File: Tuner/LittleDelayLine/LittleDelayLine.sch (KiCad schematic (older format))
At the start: 114 parts, among them J1 Conn_Coaxial, J10 Conn_Coaxial, J11 Conn_02x05_Odd_Even, J12 Conn_01x01, J13 Conn_01x01, J14 Conn_01x01, J15 Conn_01x01, J16 Conn_01x01, J17 Conn_Coaxial, J18 Conn_01x01, J19 Conn_01x01, J2 Conn_Coaxial, J20 Conn_01x01, J21 Conn_01x01, J22 Conn_Coaxial, J23 Conn_Coaxial, J24 Conn_Coaxial, J25 Conn_01x01, J26 Conn_01x01, J27 Conn_01x01, J3 Conn_Coaxial, J4 Conn_Coaxial, J5 Conn_Coaxial, J6 Conn_Coaxial, J7 Conn_Coaxial, J8 Conn_01x02, J9 Conn_01x02, P10 Conn_01x01, P11 Conn_01x01, P12 Conn_01x01, P2 Conn_01x01, P3 Conn_01x01, P4 Conn_01x01, P5 Conn_01x01, P6 Conn_01x01, P7 Conn_01x01, P8 Conn_01x01, P9 Conn_01x01, U1 MCP23008, U2 ULN2803A

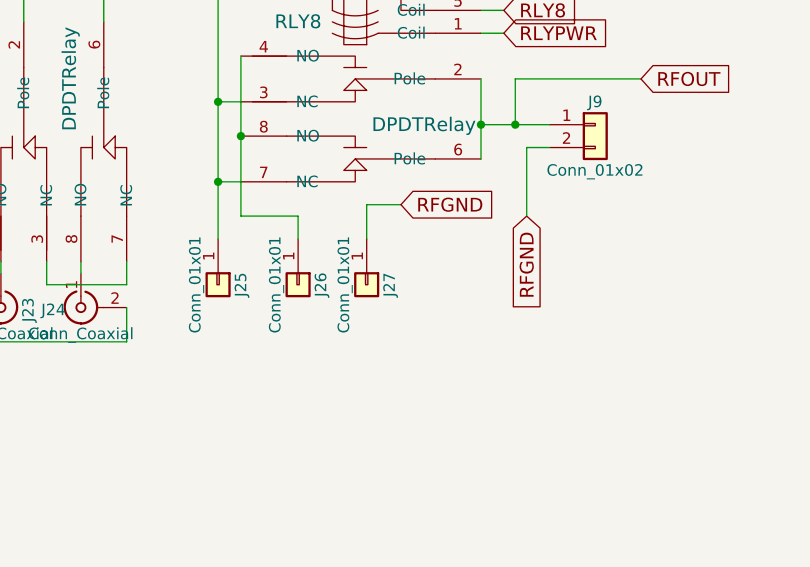
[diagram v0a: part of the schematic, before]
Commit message: Added more instrumentation to TandemMatch, fixed grounding issue
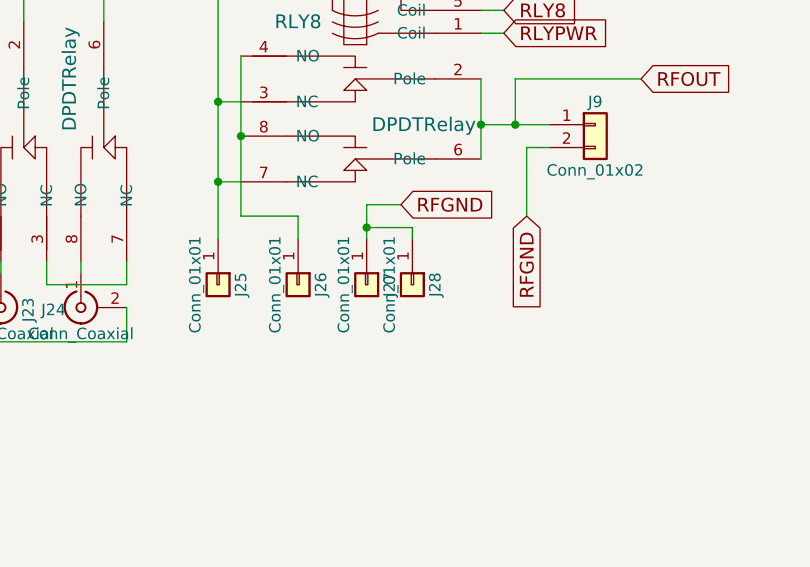
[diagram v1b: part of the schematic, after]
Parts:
- added J28: Conn_01x01, Connectors:1pin, symbol Conn_01x01
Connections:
- net RFGND: now also J28.1 (Pin_1)
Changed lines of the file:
@@
 	3150 4200 3300 4200
 Connection ~ 3300 4250
+$Comp
+L Conn_01x01 J28
+U 1 1 5C745726
+P 7950 2200
+F 0 "J28" H 7950 2300 50  0000 C CNN
+F 1 "Conn_01x01" H 7950 2100 50  0000 C CNN
+F 2 "Connectors:1pin" H 7950 2200 50  0001 C CNN
+F 3 "" H 7950 2200 50  0001 C CNN
+	1    7950 2200
+	0    1    1    0
+$EndComp
+Wire Wire Line
+	7950 2000 7950 1950
+Wire Wire Line
+	7950 1950 7750 1950
+Connection ~ 7750 1950
 $EndSCHEMATC

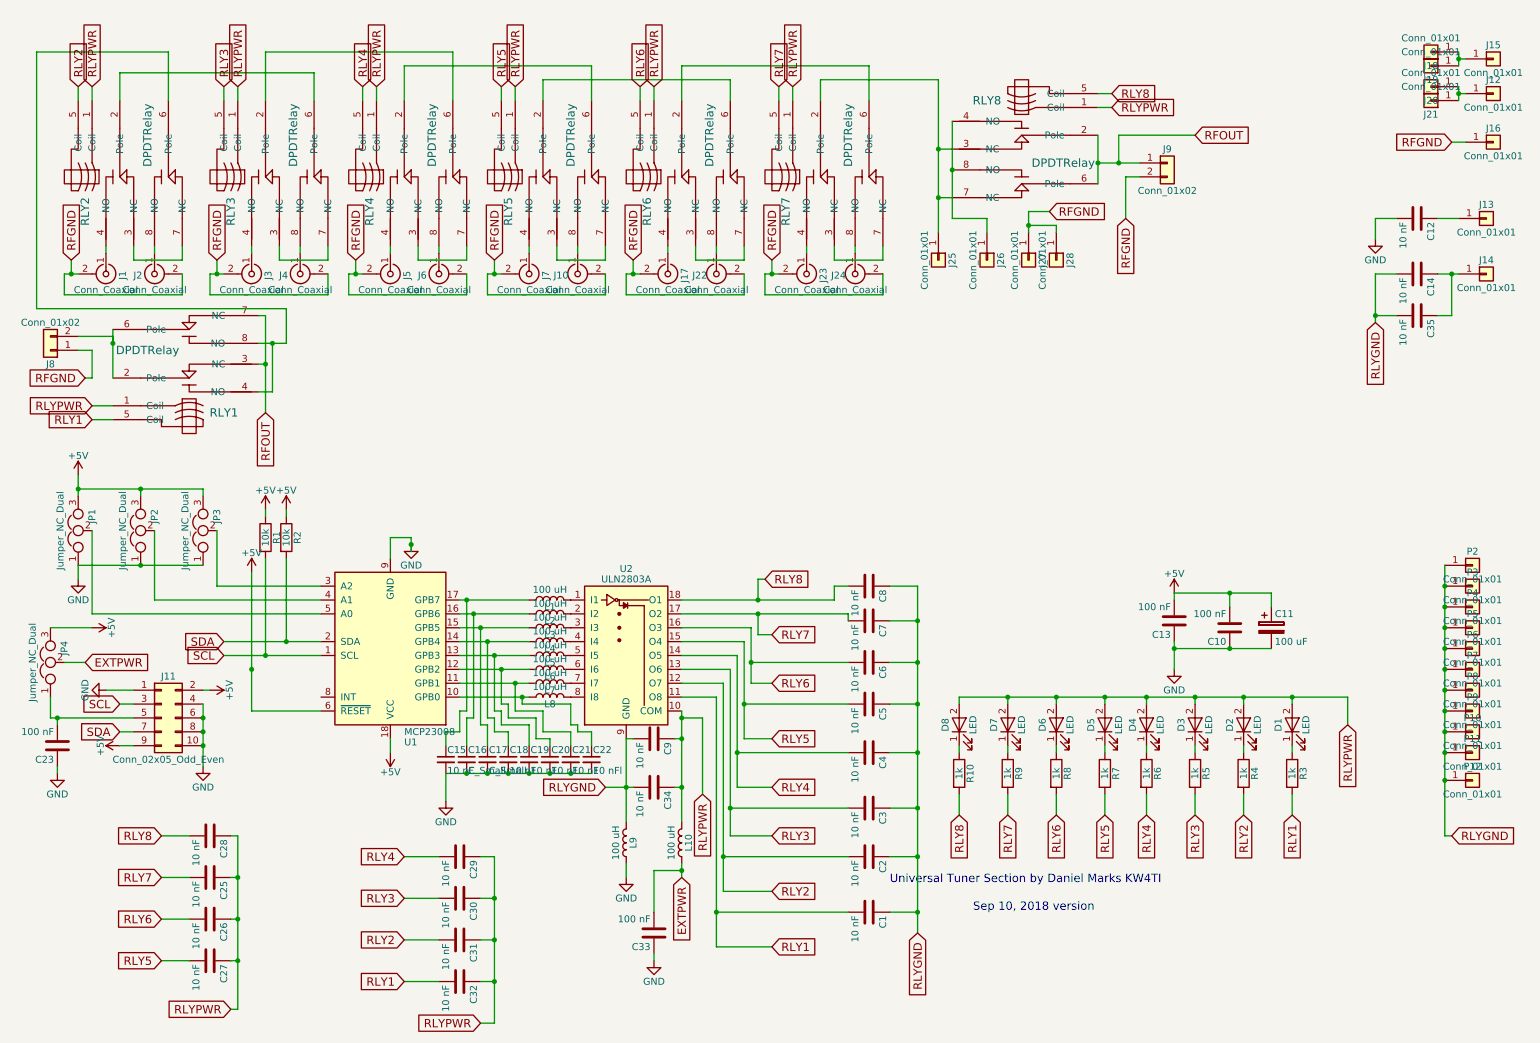
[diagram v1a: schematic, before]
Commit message: Added BNC and screw terminal combo pads
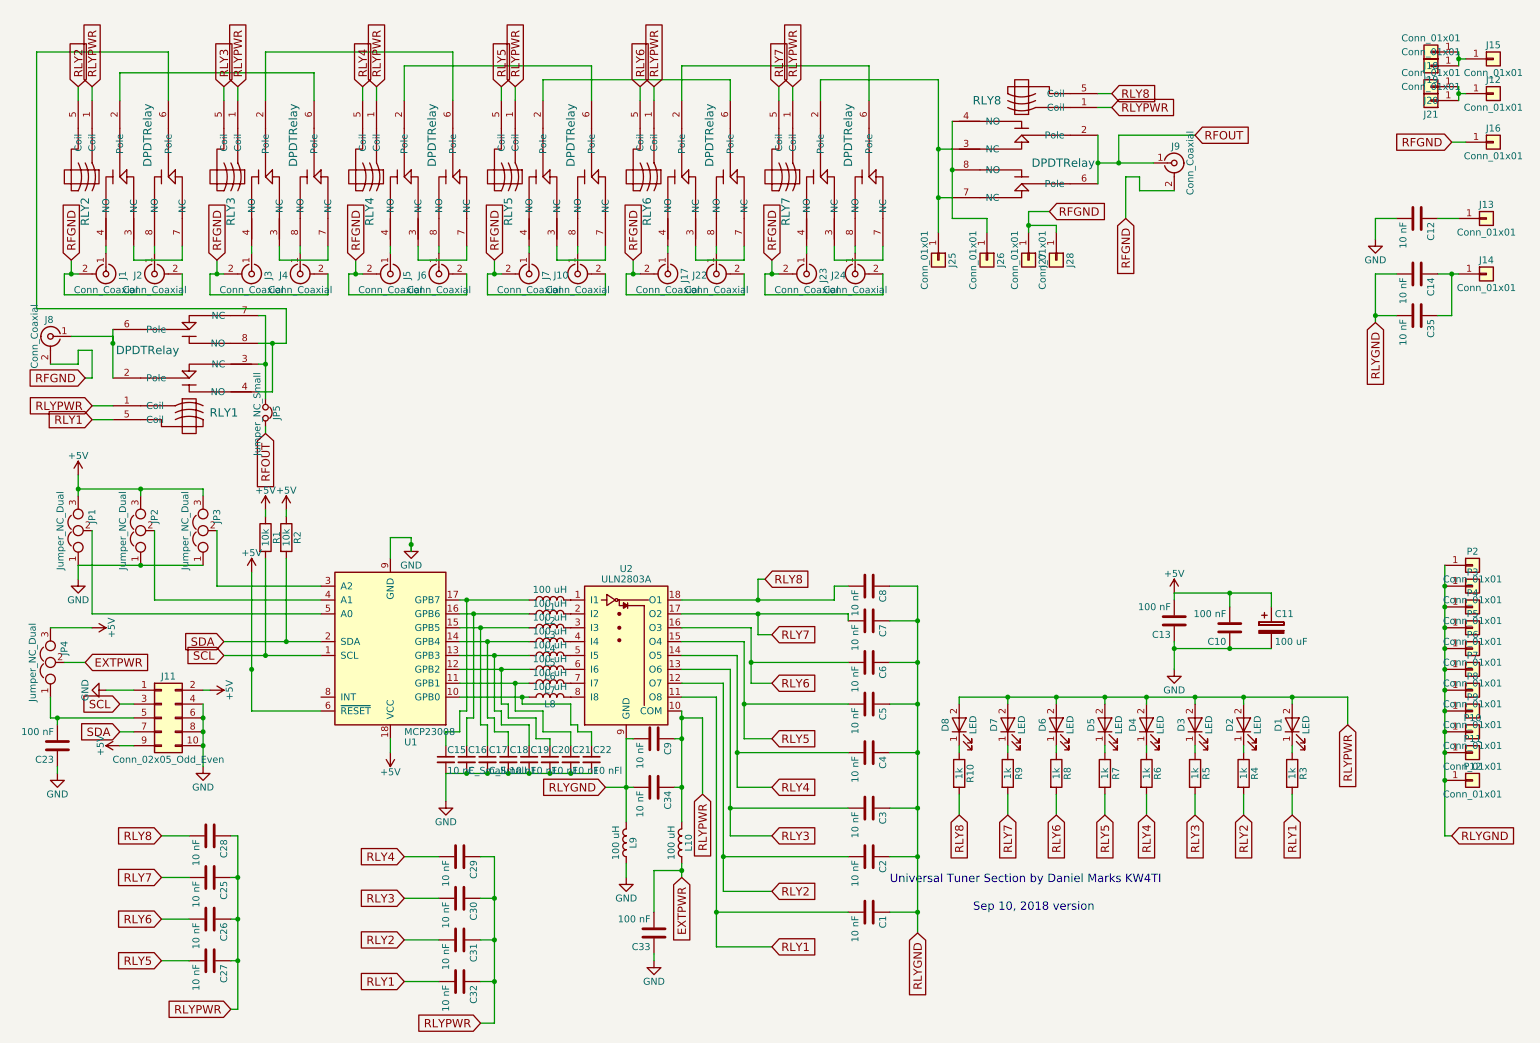
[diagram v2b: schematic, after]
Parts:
- removed J8, J9: Conn_01x02, Connectors_Terminal_Blocks:TerminalBlock_bornier-2_P5.08mm, symbol Conn_01x02
- added J8, J9: Conn_Coaxial, tuner:bnc_90_1-1337543-0_pad_combo, symbol Conn_Coaxial
- added JP5: Jumper_NC_Small, Pin_Headers:Pin_Header_Straight_1x02_Pitch2.54mm, symbol Jumper_NC_Small
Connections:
- net RFGND: now also J8.2 (Ext), J9.2 (Ext)
- net RFOUT: now also J9.1 (In), JP5.2; no longer RLY1.3 (NC), RLY1.7 (NC)
- net at RLY1.2 (Pole), RLY1.6 (Pole): now also J8.1 (In)
- new net: JP5.1, RLY1.3 (NC), RLY1.7 (NC)
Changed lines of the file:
@@
 Comment4 ""
 $EndDescr
-Text GLabel 2250 3300 3    60   Input ~ 0
+Text GLabel 2250 3450 3    60   Input ~ 0
 RFOUT
-$Comp
-L Conn_01x02 J8
-U 1 1 5B18E79B
-P 700 2850
-F 0 "J8" H 700 2950 50  0000 C CNN
-F 1 "Conn_01x02" H 700 2650 50  0000 C CNN
-F 2 "Connectors_Terminal_Blocks:TerminalBlock_bornier-2_P5.08mm" H 700 2850 50  0001 C CNN
-F 3 "" H 700 2850 50  0001 C CNN
-	1    700  2850
-	-1   0    0    1
-$EndComp
 Text GLabel 5900 7150 2    60   Input ~ 0
 RLY1
@@
 F 3 "" H 9500 4850 50  0001 C CNN
 	1    9500 4850
-	1    0    0    -1
-$EndComp
-$Comp
-L Conn_01x02 J9
-U 1 1 5B18CCC7
-P 8750 1500
-F 0 "J9" H 8750 1600 50  0000 C CNN
-F 1 "Conn_01x02" H 8750 1300 50  0000 C CNN
-F 2 "Connectors_Terminal_Blocks:TerminalBlock_bornier-2_P5.08mm" H 8750 1500 50  0001 C CNN
-F 3 "" H 8750 1500 50  0001 C CNN
-	1    8750 1500
 	1    0    0    -1
 $EndComp
@@
 	1150 2700 1150 3050
 Wire Wire Line
-	1150 2800 1150 2750
-Wire Wire Line
-	1150 2750 900  2750
+	1150 2750 1150 2800
+Wire Wire Line
+	850  2750 1150 2750
 Connection ~ 1150 2800
 Wire Wire Line
-	2250 2600 2250 3300
+	2250 2600 2250 3200
 Wire Wire Line
 	2250 2600 2200 2600
@@
 Wire Wire Line
 	4600 800  4600 1050
-Connection ~ 2250 2950
 Wire Wire Line
 	2400 2800 2400 2550
@@
 	8250 1300 8250 1650
 Wire Wire Line
-	8250 1500 8550 1500
+	8250 1500 8650 1500
 Connection ~ 8250 1500
 Wire Wire Line
@@
 	7950 1950 7750 1950
 Connection ~ 7750 1950
+$Comp
+L Conn_Coaxial J8
+U 1 1 5C7C04B6
+P 700 2750
+F 0 "J8" H 710 2870 50  0000 C CNN
+F 1 "Conn_Coaxial" V 815 2750 50  0000 C CNN
+F 2 "tuner:bnc_90_1-1337543-0_pad_combo" H 700 2750 50  0001 C CNN
+F 3 "" H 700 2750 50  0001 C CNN
+	1    700  2750
+	-1   0    0    -1
+$EndComp
+Wire Wire Line
+	900  2850 900  2950
+Wire Wire Line
+	900  2950 700  2950
+$Comp
+L Conn_Coaxial J9
+U 1 1 5C7C0EBB
+P 8800 1500
+F 0 "J9" H 8810 1620 50  0000 C CNN
+F 1 "Conn_Coaxial" V 8915 1500 50  0000 C CNN
+F 2 "tuner:bnc_90_1-1337543-0_pad_combo" H 8800 1500 50  0001 C CNN
+F 3 "" H 8800 1500 50  0001 C CNN
+	1    8800 1500
+	1    0    0    -1
+$EndComp
+Wire Wire Line
+	8550 1600 8550 1700
+Wire Wire Line
+	8550 1700 8800 1700
+$Comp
+L Jumper_NC_Small JP5
+U 1 1 5C7C4162
+P 2250 3300
+F 0 "JP5" H 2250 3380 50  0000 C CNN
+F 1 "Jumper_NC_Small" H 2260 3240 50  0000 C CNN
+F 2 "Pin_Headers:Pin_Header_Straight_1x02_Pitch2.54mm" H 2250 3300 50  0001 C CNN
+F 3 "" H 2250 3300 50  0001 C CNN
+	1    2250 3300
+	0    1    1    0
+$EndComp
+Connection ~ 2250 2950
+Wire Wire Line
+	2250 3400 2250 3450
 $EndSCHEMATC

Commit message: Changed bypass method on delay lines
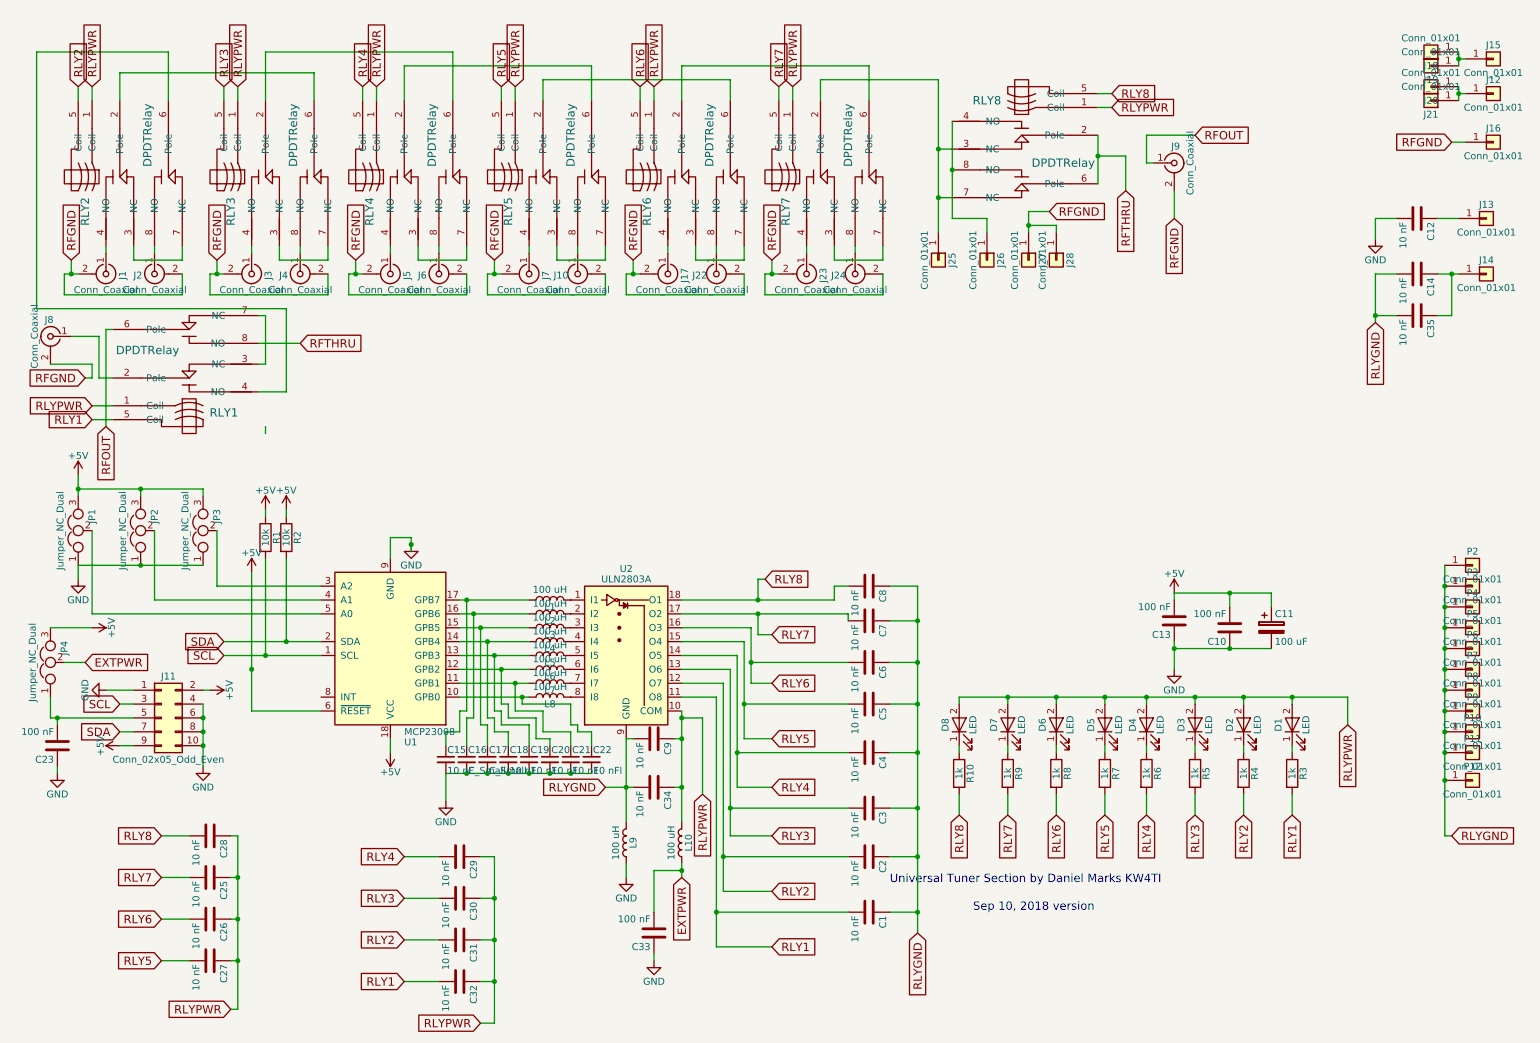
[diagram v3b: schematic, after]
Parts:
- removed JP5: Jumper_NC_Small, Pin_Headers:Pin_Header_Straight_1x02_Pitch2.54mm, symbol Jumper_NC_Small
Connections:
- net RFOUT: now also RLY1.6 (Pole); no longer RLY8.2 (Pole), RLY8.6 (Pole)
- net at J8.1 (In), RLY1.2 (Pole): no longer RLY1.6 (Pole)
- net at RLY1.4 (NO), RLY2.6 (Pole): no longer RLY1.8 (NO)
- new net RFTHRU: RLY1.8 (NO), RLY8.2 (Pole), RLY8.6 (Pole)
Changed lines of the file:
@@
 Comment4 ""
 $EndDescr
-Text GLabel 2250 3450 3    60   Input ~ 0
+Text GLabel 1100 3400 3    60   Input ~ 0
 RFOUT
 Text GLabel 5900 7150 2    60   Input ~ 0
@@
 	1    0    0    -1
 $EndComp
-$Comp
-L DPDTRelay RLY1
-U 1 1 5C74004F
-P 1700 3150
-F 0 "RLY1" H 1950 3000 60  0000 C CNN
-F 1 "DPDTRelay" H 1400 3450 60  0000 C CNN
-F 2 "tuner:G2VRelay" H 1700 3150 60  0001 C CNN
-F 3 "" H 1700 3150 60  0001 C CNN
-	1    1700 3150
-	1    0    0    -1
-$EndComp
 Text GLabel 1000 3350 0    60   Input ~ 0
 RLY1
@@
 Text GLabel 7900 1850 2    60   Input ~ 0
 RFGND
-Text GLabel 8450 1900 3    60   Input ~ 0
+Text GLabel 8800 1900 3    60   Input ~ 0
 RFGND
 Connection ~ 9650 5350
@@
 	950  3050 1000 3050
 Wire Wire Line
-	1000 3050 1000 2850
-Wire Wire Line
-	1000 2850 900  2850
-Wire Wire Line
-	1150 2700 1150 3050
-Wire Wire Line
-	1150 2750 1150 2800
-Wire Wire Line
-	850  2750 1150 2750
-Connection ~ 1150 2800
-Wire Wire Line
-	2250 2600 2250 3200
+	1000 3050 1000 2950
+Wire Wire Line
+	2250 2600 2250 2950
 Wire Wire Line
 	2250 2600 2200 2600
@@
 	2250 2950 2200 2950
 Wire Wire Line
-	2200 2800 2400 2800
-Wire Wire Line
-	2300 2800 2300 3150
-Wire Wire Line
-	2300 3150 2200 3150
-Connection ~ 2300 2800
+	2400 3150 2200 3150
 Wire Wire Line
 	1000 950  1000 1050
@@
 	4600 800  4600 1050
 Wire Wire Line
-	2400 2800 2400 2550
+	2400 2550 2400 3150
 Wire Wire Line
 	2400 2550 600  2550
@@
 	8250 1300 8250 1650
 Wire Wire Line
-	8250 1500 8650 1500
-Connection ~ 8250 1500
+	8600 1500 8650 1500
 Wire Wire Line
 	7900 1850 7750 1850
 Wire Wire Line
 	7750 1850 7750 2000
-Wire Wire Line
-	8450 1900 8450 1600
-Wire Wire Line
-	8450 1600 8550 1600
 Text GLabel 8950 1300 2    60   Input ~ 0
 RFOUT
 Wire Wire Line
-	8950 1300 8400 1300
-Wire Wire Line
-	8400 1300 8400 1500
-Connection ~ 8400 1500
+	8950 1300 8600 1300
 $Comp
 L R R1
@@
 $EndComp
 Wire Wire Line
-	900  2850 900  2950
-Wire Wire Line
-	900  2950 700  2950
+	1000 2950 700  2950
 $Comp
 L Conn_Coaxial J9
@@
 $EndComp
 Wire Wire Line
-	8550 1600 8550 1700
-Wire Wire Line
-	8550 1700 8800 1700
-$Comp
-L Jumper_NC_Small JP5
-U 1 1 5C7C4162
-P 2250 3300
-F 0 "JP5" H 2250 3380 50  0000 C CNN
-F 1 "Jumper_NC_Small" H 2260 3240 50  0000 C CNN
-F 2 "Pin_Headers:Pin_Header_Straight_1x02_Pitch2.54mm" H 2250 3300 50  0001 C CNN
-F 3 "" H 2250 3300 50  0001 C CNN
-	1    2250 3300
-	0    1    1    0
-$EndComp
-Connection ~ 2250 2950
-Wire Wire Line
 	2250 3400 2250 3450
+Wire Wire Line
+	8600 1300 8600 1500
+Wire Wire Line
+	8800 1700 8800 1900
+Text GLabel 8450 1700 3    60   Input ~ 0
+RFTHRU
+Wire Wire Line
+	8450 1700 8450 1450
+Wire Wire Line
+	8450 1450 8250 1450
+Connection ~ 8250 1450
+$Comp
+L DPDTRelay RLY1
+U 1 1 5C74004F
+P 1700 3150
+F 0 "RLY1" H 1950 3000 60  0000 C CNN
+F 1 "DPDTRelay" H 1400 3450 60  0000 C CNN
+F 2 "tuner:G2VRelay" H 1700 3150 60  0001 C CNN
+F 3 "" H 1700 3150 60  0001 C CNN
+	1    1700 3150
+	1    0    0    -1
+$EndComp
+Wire Wire Line
+	1150 3050 1050 3050
+Wire Wire Line
+	1050 3050 1050 2750
+Wire Wire Line
+	1050 2750 850  2750
+Wire Wire Line
+	1100 3400 1100 2700
+Wire Wire Line
+	1100 2700 1150 2700
+Text GLabel 2500 2800 2    60   Input ~ 0
+RFTHRU
+Wire Wire Line
+	2500 2800 2200 2800
 $EndSCHEMATC

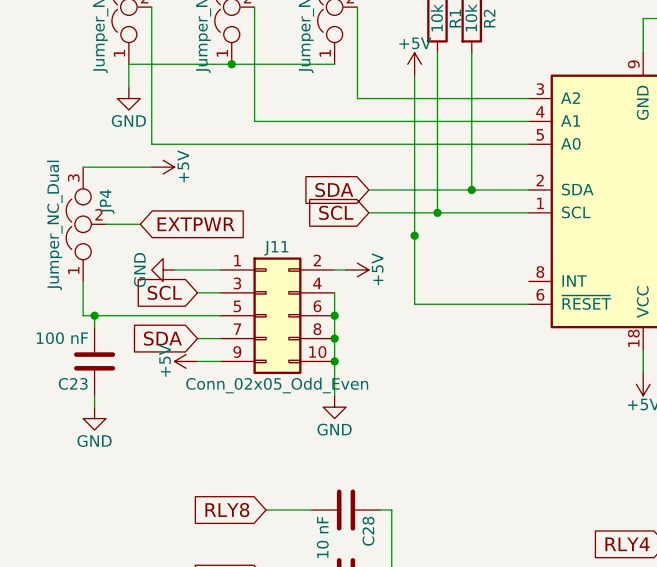
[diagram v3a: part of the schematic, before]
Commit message: Changed I2C cable pinoutgit add Tunergit add Tuner Also added ICOM rig support
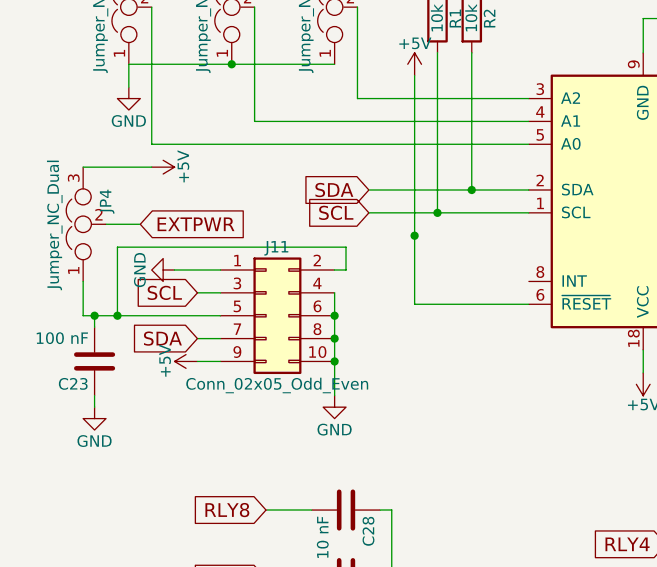
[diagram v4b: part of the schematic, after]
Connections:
- net +5V: no longer J11.2 (Pin_2)
- net at C23.2, J11.5 (Pin_5), JP4.1: now also J11.2 (Pin_2)
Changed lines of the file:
@@
-$EndComp
-$Comp
-L +5V #PWR8
-U 1 1 5BA4E273
-P 1850 5300
-F 0 "#PWR8" H 1850 5150 50  0001 C CNN
-F 1 "+5V" H 1850 5440 50  0000 C CNN
-F 2 "" H 1850 5300 50  0001 C CNN
-F 3 "" H 1850 5300 50  0001 C CNN
-	1    1850 5300
-	0    1    1    0
 $EndComp
 $Comp
@@
 Wire Wire Line
 	2500 2800 2200 2800
+Wire Wire Line
+	850  5500 850  5200
+Wire Wire Line
+	850  5200 1850 5200
+Wire Wire Line
+	1850 5200 1850 5300
+Connection ~ 850  5500
 $EndSCHEMATC
